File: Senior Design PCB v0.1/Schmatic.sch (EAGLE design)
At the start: 213 parts, among them IC1 TMC2208, IC2 TMC2208, IC3 TMC2208, IC4 TMC2208, IC5 TMC2208, IC6 CP2104, J1 XT60PW-M, J3 XT60PW-M, Q1 mmbt2222, Q2 mmbt2222, Q3 MMBT4403, Q4 AOD417, Q5 MMBT4403, Q6 MMBT4403, Q7 DMG3415U, U1 PCA9685, U2 AP2112-3.3, U3 HTU21DF, U4 HX711, U5 HX711, U6 HX711, X2 ESP32_WROOM32_SKINNY

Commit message: done layout, waiting for signal wire pin config
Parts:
- removed FAN, VIBRATION: S2B-PH-SM4_TB, NewKevinMade:S2B-PH-SM4_TB
- added C67, C69, C70, C71, C72, C73: 100uF, SparkFun-Capacitors:100UF-POLAR-25V-20%(ELEC)
- added C68: 560uF, SparkFun-Capacitors:560UF-PANASONIC_G-25V-20%
- added D7, D8: RED, microbuilder:LED0805_NOOUTLINE
- added FAN_, VIBRATION_: B2B-PH-SM4-TB(LF)(SN), B2B-PH-SM4-TB_LF__SN_:B2B-PH-SM4-TB(LF)(SN)
- added R70, R86: 1K, microbuilder:RESISTOR_0603_NOOUT
- added STEPPER1, STEPPER2, STEPPER3, STEPPER4, STEPPER5: S4B-PH-SM4_TB, NewKevinMade:S4B-PH-SM4_TB
- added U$48, U$49, U$50: MOUNTINGHOLE2.5, microbuilder:MOUNTINGHOLE2.5
- added WEIGHT_SENSOR: S5B-PH-SM4_TB, NewKevinMade:S5B-PH-SM4_TB
- C3: value (none) -> 560uF; device adafruit:CPOL-USE3.5-8 -> SparkFun-Capacitors:560UF-PANASONIC_G-25V-20%
- C66: value 560uF -> 100uF; device SparkFun-Capacitors:560UF-PANASONIC_G-25V-20% -> SparkFun-Capacitors:100UF-POLAR-25V-20%(ELEC)
- LIQUID_RELEASE_SW, SOLID_RELEASE_SW, X-HOMING-SW, Y-HOMING-SW: value S2B-PH-SM4_TB -> B2B-PH-SM4-TB(LF)(SN); device NewKevinMade:S2B-PH-SM4_TB -> B2B-PH-SM4-TB_LF__SN_:B2B-PH-SM4-TB(LF)(SN)
- ROTARY_SWITCH: value S5B-PH-SM4_TB -> B5B-PH-SM4-TB; device NewKevinMade:S5B-PH-SM4_TB -> B2B-PH-SM4-TB_LF__SN_:B5B-PH-SM4-TB
- U$4: value S5B-PH-SM4_TB -> MOUNTINGHOLE2.5; device NewKevinMade:S5B-PH-SM4_TB -> microbuilder:MOUNTINGHOLE2.5
- renumbered J1 to 12V_IN, J3 to 5V_IN
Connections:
- removed net N$29: X-HOMING-SW.JST2
- removed net N$30: X-HOMING-SW.JST3
- removed net N$31: Y-HOMING-SW.JST2
- removed net N$32: Y-HOMING-SW.JST3
- new net N$53: D7.A, R70.2
- new net N$55: D8.A, R86.2
- new net X-HOMING: R70.1, X-HOMING-SW.2
- new net Y-HOMING: R86.1, Y-HOMING-SW.2
- net 12V_REG: now also C69.+, C70.+, C71.+, C72.+, C73.+
- net 5V_REG: now also FAN_.2, VIBRATION_.2; no longer FAN.JST3, VIBRATION.JST3
- net 5V_SERVO: now also C68.+
- net A+_2: now also WEIGHT_SENSOR.JST4; no longer U$4.JST4
- net A-_2: now also WEIGHT_SENSOR.JST3; no longer U$4.JST3
- net AVDD_2: now also WEIGHT_SENSOR.JST1; no longer U$4.JST1
- net FAN_5V: now also FAN_.1; no longer FAN.JST2
- net GND: now also C67.-, C68.-, C69.-, C70.-, C71.-, C72.-, C73.-, D7.C, D8.C, ROTARY_SWITCH.2, ROTARY_SWITCH.4, WEIGHT_SENSOR.JST2, WEIGHT_SENSOR.JST5; no longer ROTARY_SWITCH.JST2, ROTARY_SWITCH.JST4, U$4.JST2, U$4.JST5
- net LRSW: now also LIQUID_RELEASE_SW.2; no longer LIQUID_RELEASE_SW.JST3
- net OA1_1: now also STEPPER1.JST1
- net OA1_2: now also STEPPER2.JST1
- net OA1_3: now also STEPPER3.JST1
- net OA1_4: now also STEPPER4.JST1
- net OA1_5: now also STEPPER5.JST1
- net OA2_1: now also STEPPER1.JST2
- net OA2_2: now also STEPPER2.JST2
- net OA2_3: now also STEPPER3.JST2
- net OA2_4: now also STEPPER4.JST2
- net OA2_5: now also STEPPER5.JST2
- net OB1_1: now also STEPPER1.JST3
- net OB1_2: now also STEPPER2.JST3
- net OB1_3: now also STEPPER3.JST3
- net OB1_4: now also STEPPER4.JST3
- net OB1_5: now also STEPPER5.JST3
- net OB2_1: now also STEPPER1.JST4
- net OB2_2: now also STEPPER2.JST4
- net OB2_3: now also STEPPER3.JST4
- net OB2_4: now also STEPPER4.JST4
- net OB2_5: now also STEPPER5.JST4
- net ROTA_A: now also ROTARY_SWITCH.1; no longer ROTARY_SWITCH.JST1
- net ROTA_C: now also ROTARY_SWITCH.3; no longer ROTARY_SWITCH.JST3
- net ROTA_E: now also ROTARY_SWITCH.5; no longer ROTARY_SWITCH.JST5
- net SRSW: now also SOLID_RELEASE_SW.2; no longer SOLID_RELEASE_SW.JST3
- net VCC: now also C67.+, LIQUID_RELEASE_SW.1, SOLID_RELEASE_SW.1, X-HOMING-SW.1, Y-HOMING-SW.1; no longer LIQUID_RELEASE_SW.JST2, SOLID_RELEASE_SW.JST2
- net VIB_5V: now also VIBRATION_.1; no longer VIBRATION.JST2
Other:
- moved on the sheet: C3, C66

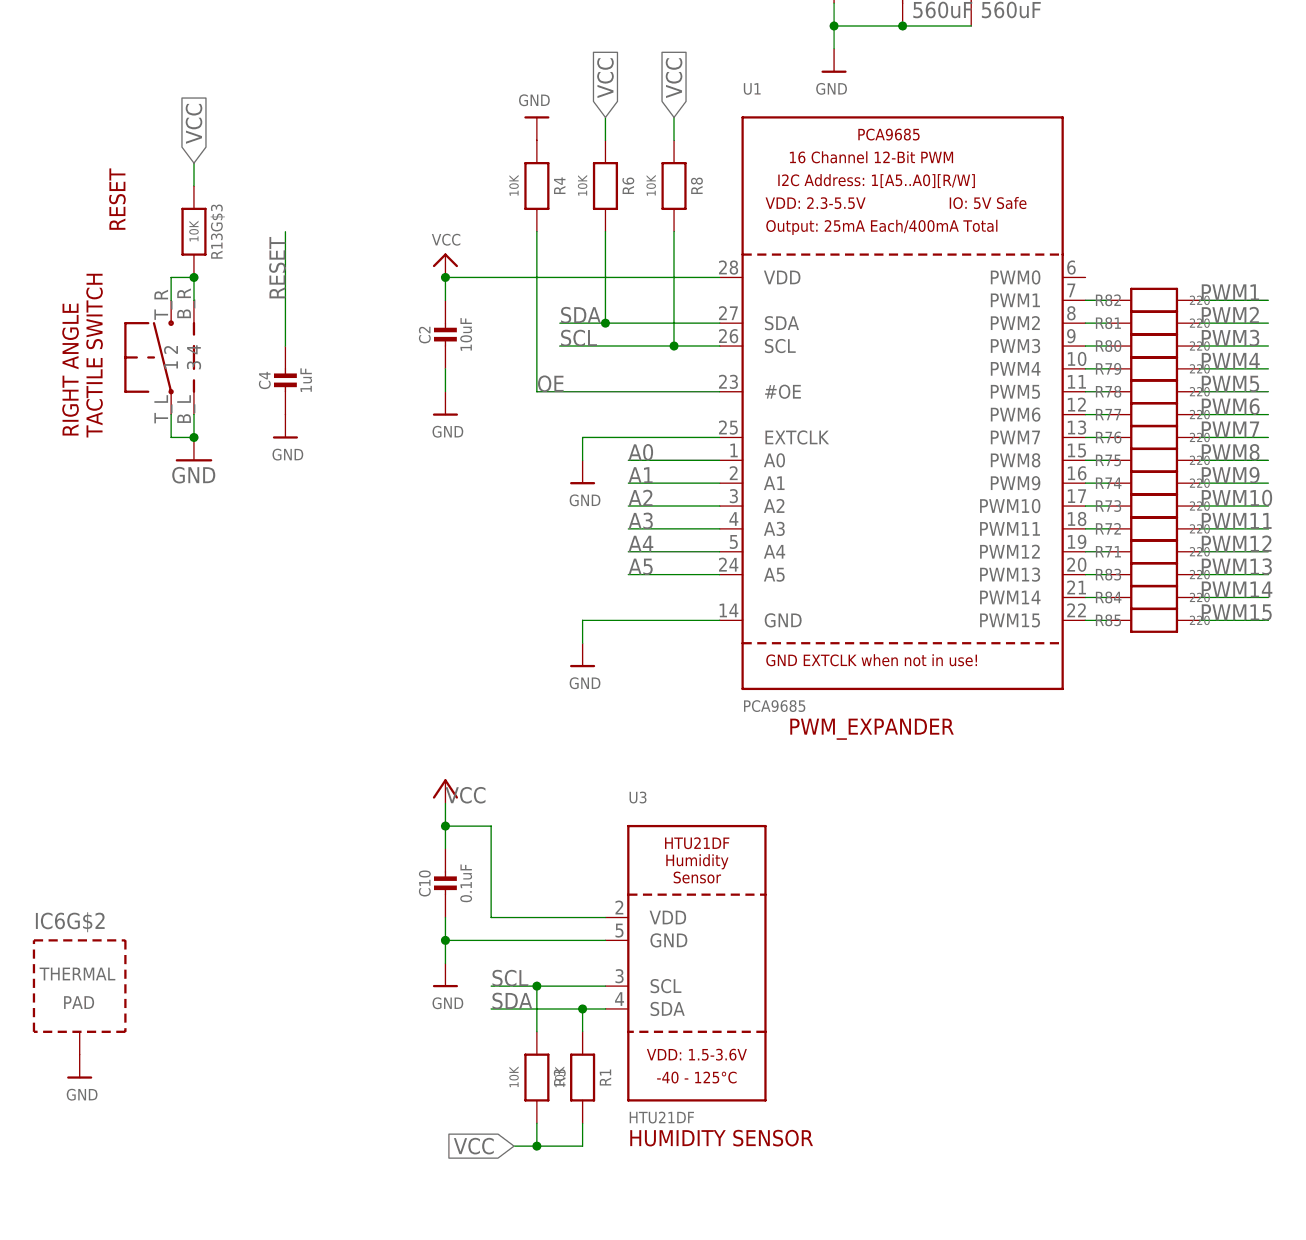
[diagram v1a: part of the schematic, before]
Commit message: update pcb layout, finishedd net class assignment. assigned gnd plane, signal plane and Vref plane
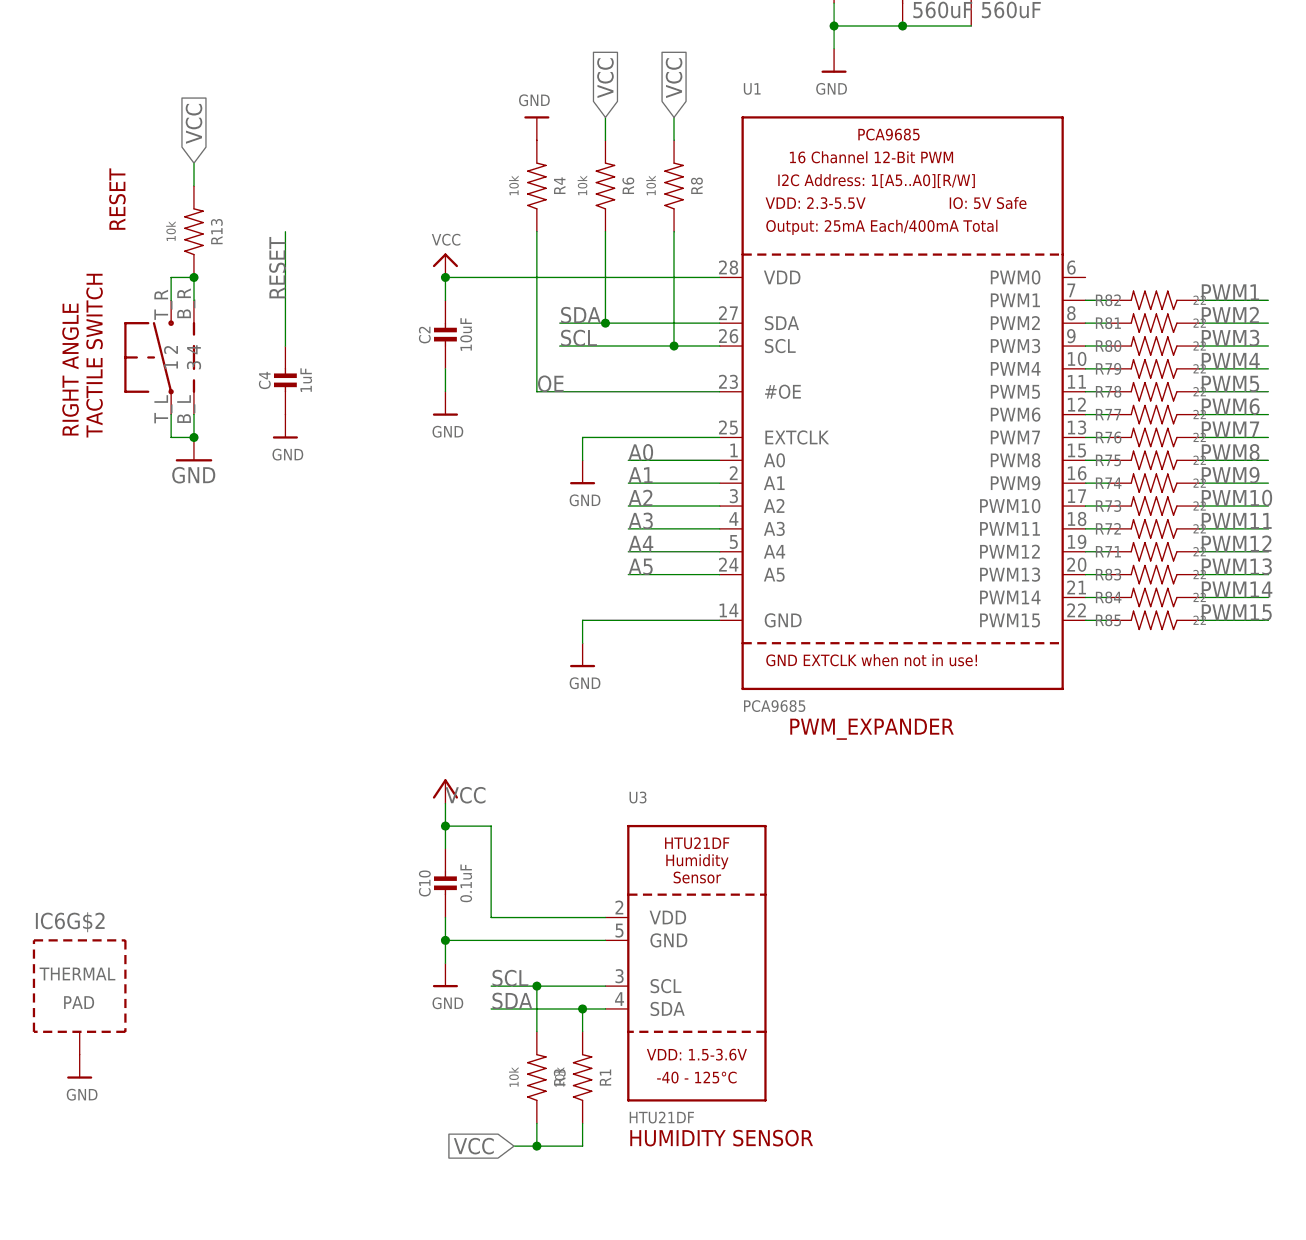
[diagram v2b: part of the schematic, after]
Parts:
- R1, R3, R4, R6, R8: value 10K -> 10k; device microbuilder:RESISTOR0805_NOOUTLINE -> SparkFun-Resistors:10KOHM-0603-1/10W-1%
- R13: value 10K -> 10k; device microbuilder:RESISTOR_4PACK -> SparkFun-Resistors:10KOHM-0603-1/10W-1%
- R71, R72, R73, R74, R75, R76, R77, R78, R79, R80, R81, R82, R83, R84, R85: value 220 -> 22; device microbuilder:RESISTOR0805_NOOUTLINE -> SparkFun-Resistors:22OHM-0603-1/10W-1%
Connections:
- net N$54: now also R13.1; no longer R13G$3.2
- net VCC: now also R13.2; no longer R13G$3.1
